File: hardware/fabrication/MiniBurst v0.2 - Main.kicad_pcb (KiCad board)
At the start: 2 copper layers, 65 x 128.5 mm, 79 parts, among them J1 TRIG_IN, J2 TRIG_OUT, J3 EXT_CLK, J4 DURATION_OUT, J5 END_OUT, J6 PULSES_OUT, J7 Conn_01x10_Pin, SW2 STEPS, SW3 SW_DPDT_x2, U1 LM358, U2 40106, U3 4017, U4 LM358, U5 LM358

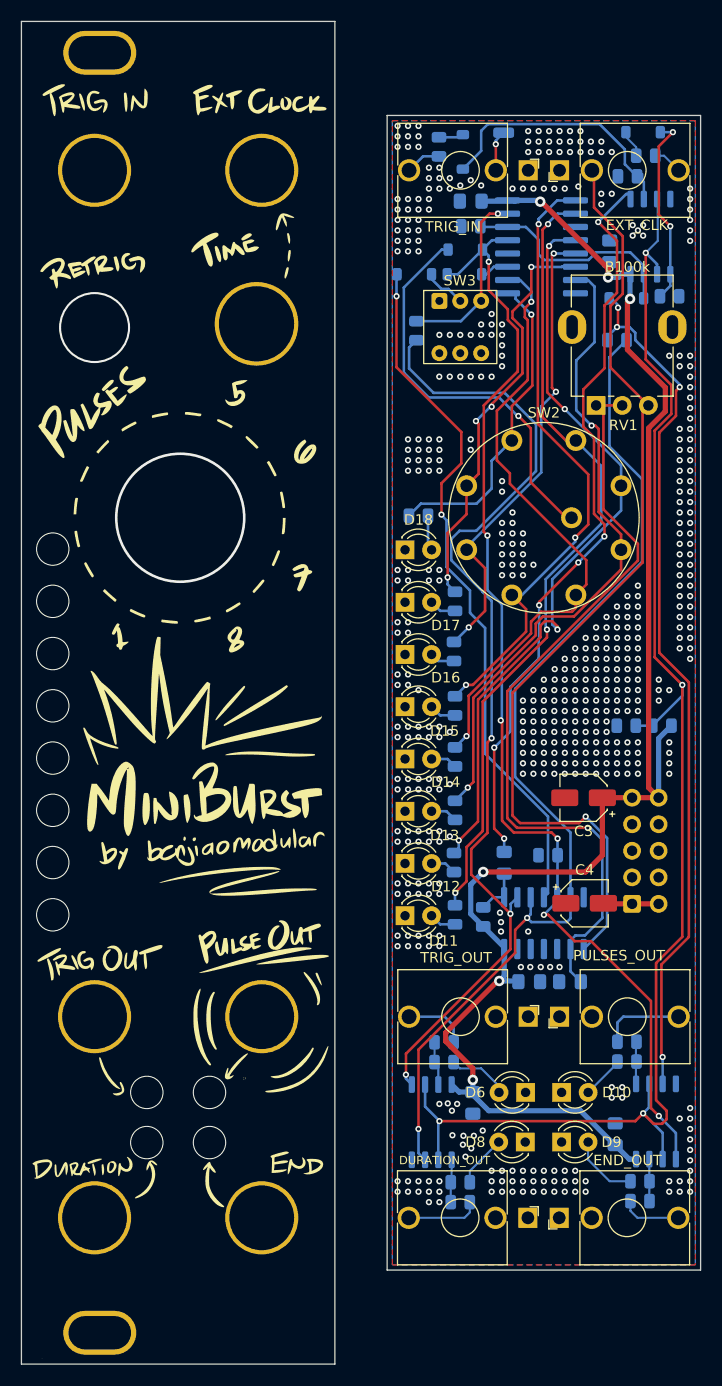
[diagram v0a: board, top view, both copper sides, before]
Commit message: Adjusted main pcb dimensions to fit 3d printed rails
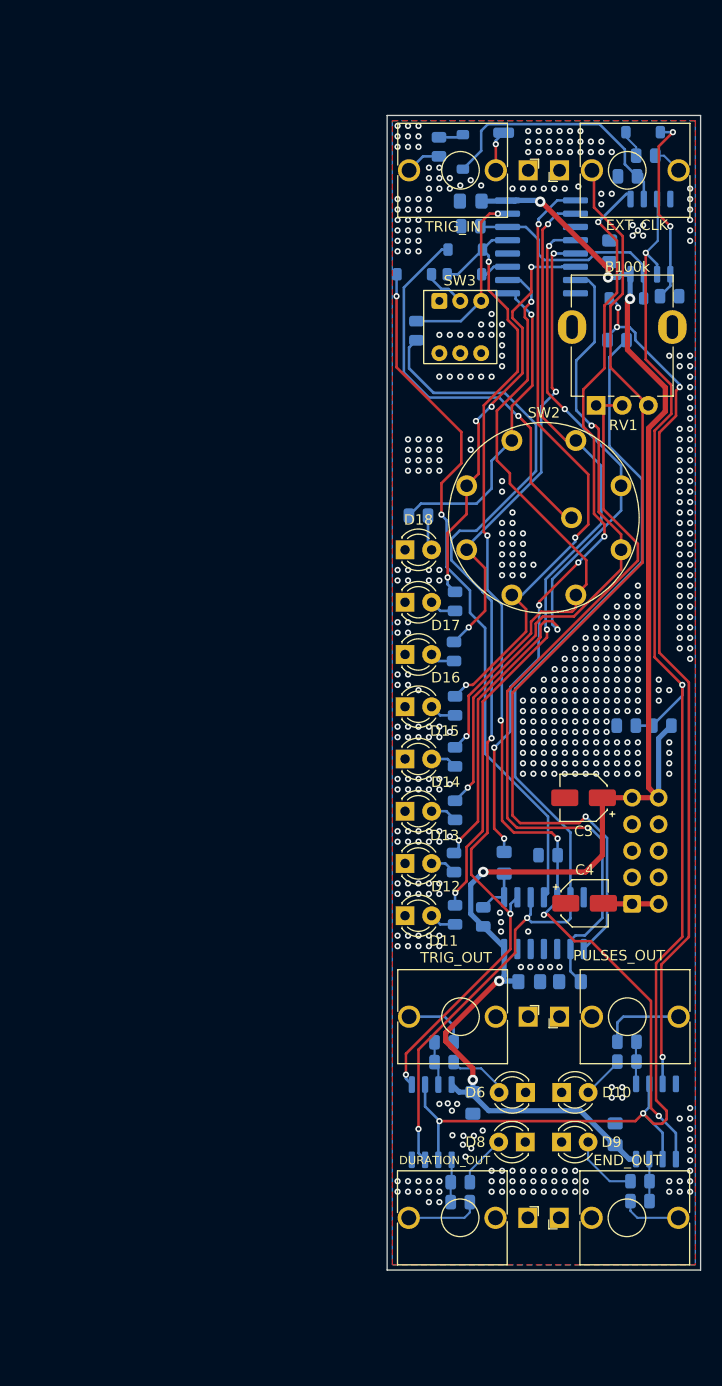
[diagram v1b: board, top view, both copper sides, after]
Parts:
- removed G***: LOGO, LOGO
- removed REF** (x6): PanelHole_AudioJack_3.5mm, benjiaomodular:PanelHole_AudioJack_3.5mm
- removed REF**: Panel_6HP, benjiaomodular:Panel_6HP
- removed REF**: PanelHole_Potentiometer_RV09, benjiaomodular:PanelHole_Potentiometer_RV09
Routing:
- net (no net): vias 14 -> 0
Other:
- board size 65 x 128.5 mm -> 30 x 110.5 mm
